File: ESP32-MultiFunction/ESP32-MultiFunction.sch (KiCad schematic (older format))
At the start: 8 parts, among them U0 ESP32_DEVKIT_C

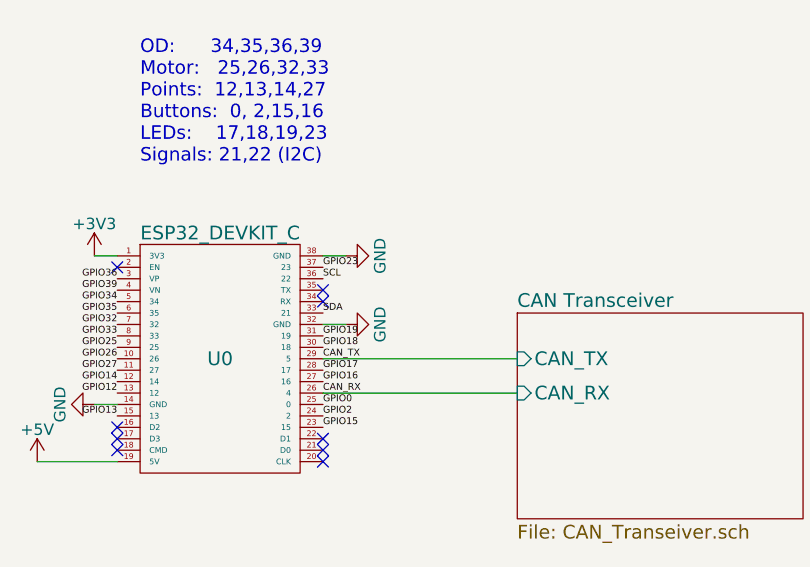
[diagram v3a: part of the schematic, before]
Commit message: Add I2C pullups to ESP32-MultiFunction.
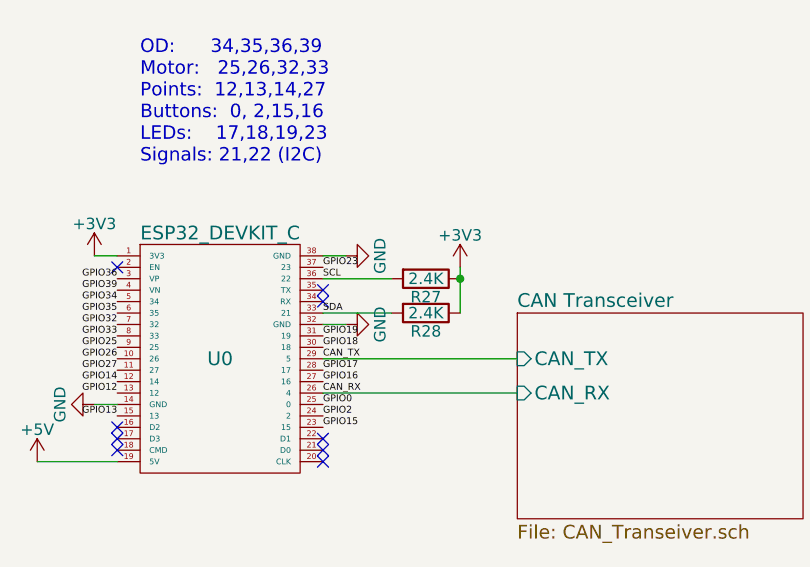
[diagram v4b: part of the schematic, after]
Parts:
- added R27, R28: 2.4K, Resistors_SMD:R_0603, symbol R
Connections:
- net +3V3: now also R27.1, R28.1
- net SCL: now also R27.2
- net SDA: now also R28.2
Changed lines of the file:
@@
 Text Label 3600 6350 0    60   ~ 0
 GPIO23
+$Comp
+L R R27
+U 1 1 61DDC30B
+P 4250 2100
+F 0 "R27" V 4330 2100 50  0000 C CNN
+F 1 "2.4K" V 4250 2100 50  0000 C CNN
+F 2 "Resistors_SMD:R_0603" V 4180 2100 50  0001 C CNN
+F 3 "" H 4250 2100 50  0001 C CNN
+F 4 "71-CRCW06032K40JN" V 4250 2100 60  0001 C CNN "Mouser Part Number"
+	1    4250 2100
+	0    1    1    0
+$EndComp
+$Comp
+L R R28
+U 1 1 61DDC4E0
+P 4250 2250
+F 0 "R28" V 4330 2250 50  0000 C CNN
+F 1 "2.4K" V 4250 2250 50  0000 C CNN
+F 2 "Resistors_SMD:R_0603" V 4180 2250 50  0001 C CNN
+F 3 "" H 4250 2250 50  0001 C CNN
+F 4 "71-CRCW06032K40JN" V 4250 2250 60  0001 C CNN "Mouser Part Number"
+	1    4250 2250
+	0    1    1    0
+$EndComp
+Wire Wire Line
+	4100 2100 3800 2100
+Wire Wire Line
+	4100 2250 3800 2250
+Wire Wire Line
+	4400 2050 4400 2250
+$Comp
+L +3V3 #PWR07
+U 1 1 61DDC7BA
+P 4400 2050
+F 0 "#PWR07" H 4400 1900 50  0001 C CNN
+F 1 "+3V3" H 4400 2190 50  0000 C CNN
+F 2 "" H 4400 2050 50  0001 C CNN
+F 3 "" H 4400 2050 50  0001 C CNN
+	1    4400 2050
+	1    0    0    -1
+$EndComp
+Connection ~ 4400 2100
 $EndSCHEMATC
